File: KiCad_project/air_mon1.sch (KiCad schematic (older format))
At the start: 36 parts, among them J1 USB_OTG, J2 Conn_01x06_Female, M1 Fan, Q1 2N7000, Q2 2N7000, SW1 SW_SPST, U1 LF33_TO220, U2 MH-Z19, U3 AM2320, U4 MSP430G2553_PW20

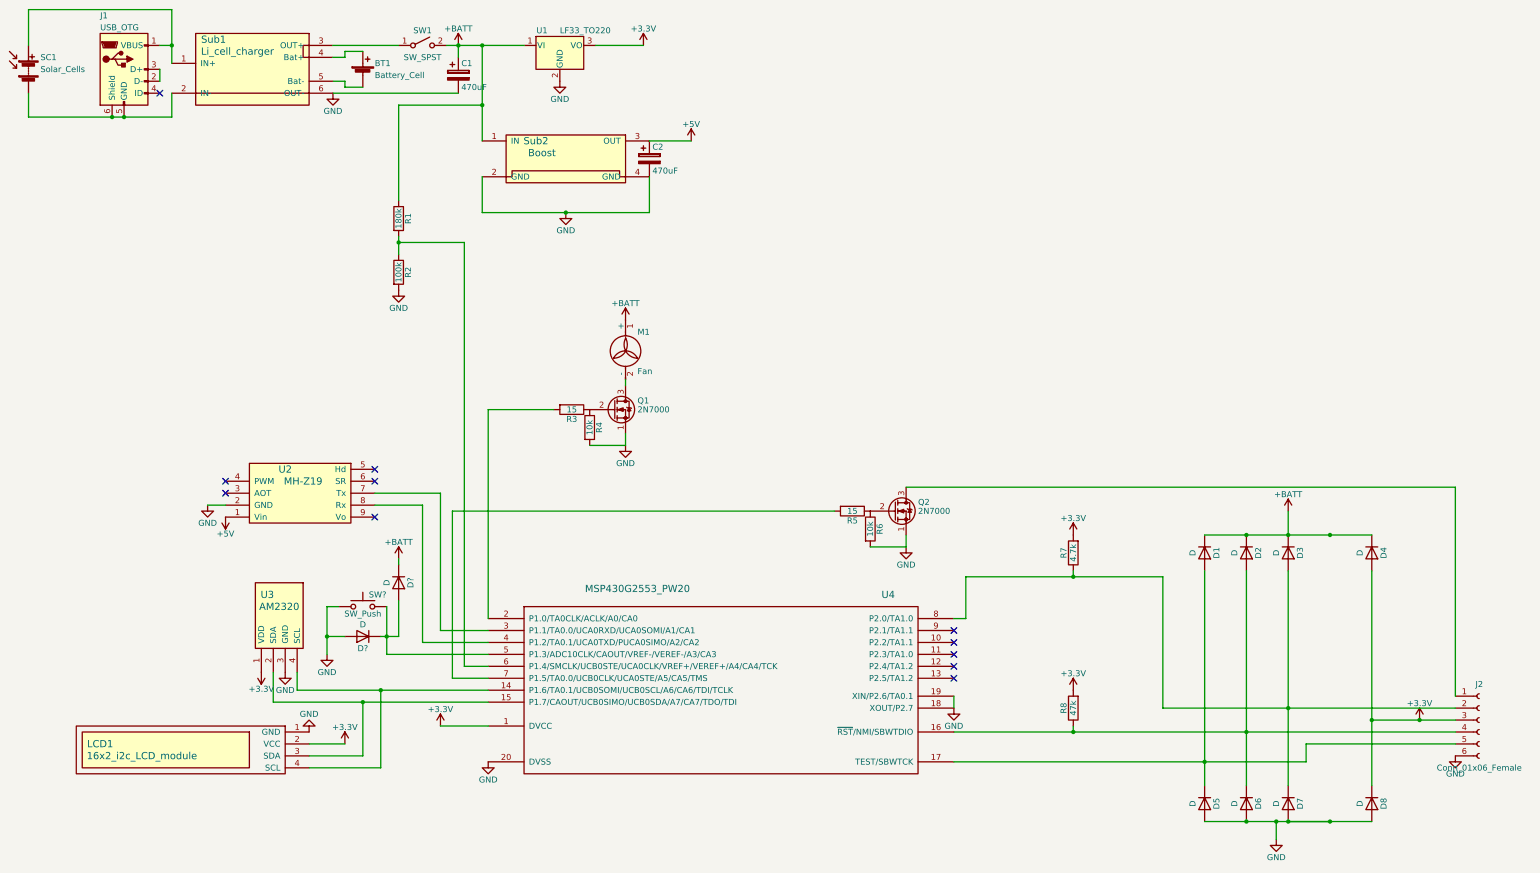
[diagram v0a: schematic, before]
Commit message: Replaced boost module
Use step-up module with Enable pin to control power of CO2 sensor
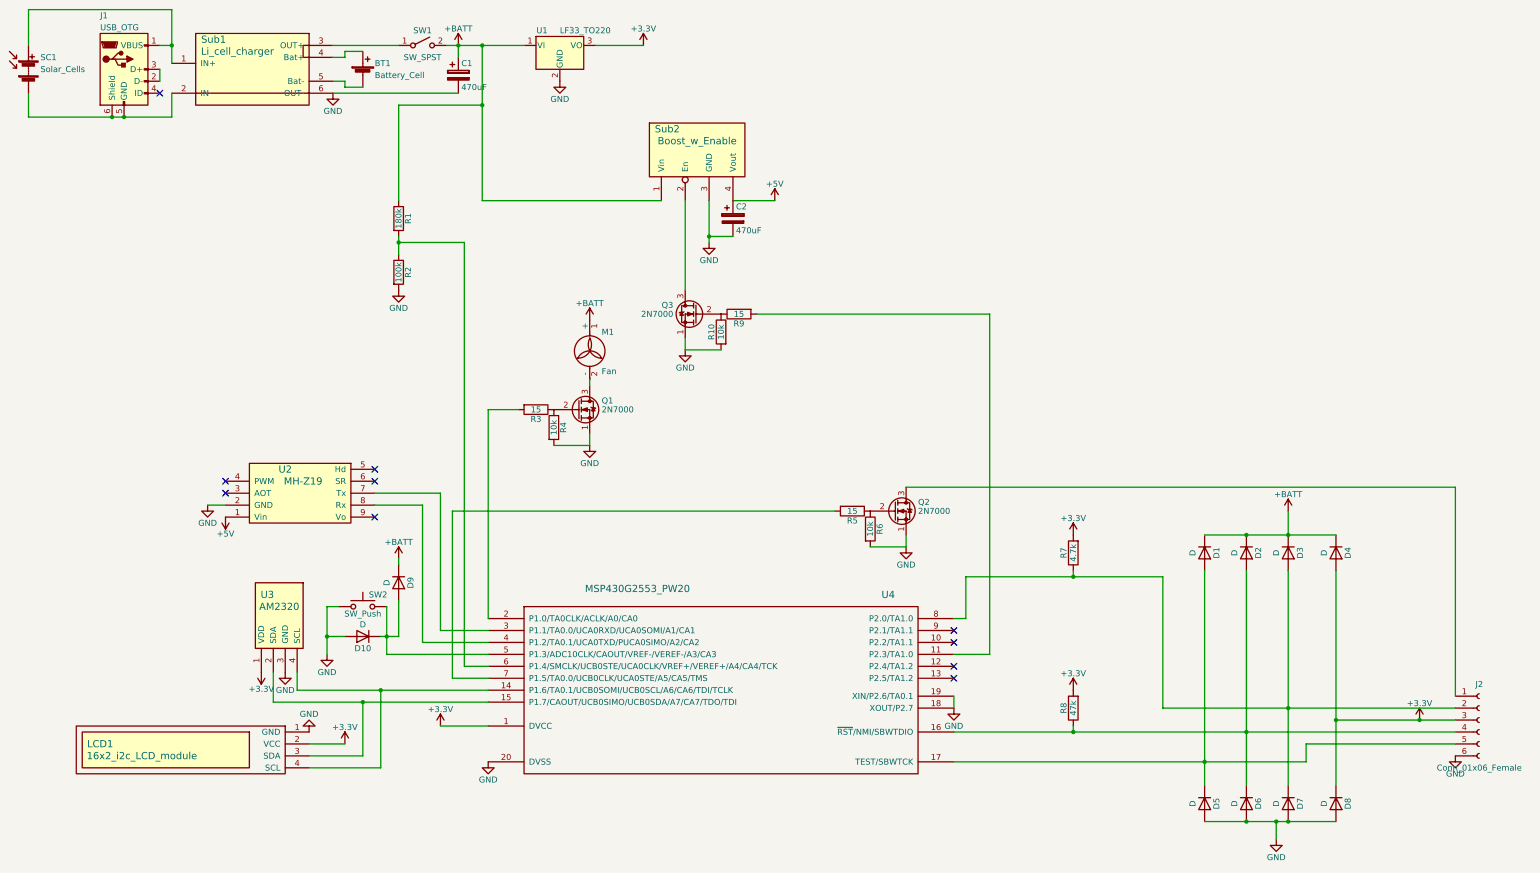
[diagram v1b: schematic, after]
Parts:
- removed Sub2: Boost, symbol Boost
- added Q3: 2N7000, TO_SOT_Packages_THT:TO-92_Molded_Narrow, symbol 2N7000
- added R10: 10k, symbol R
- added R9: 15, symbol R
- added Sub2: Boost_w_Enable, symbol Boost_w_Enable
- gave numbers to parts that had none: 3
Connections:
- net +5V: now also Sub2.4 (Vout)
- net +BATT: now also Sub2.1 (Vin)
- net GND: now also Q3.1 (S), R10.2, Sub2.3 (GND)
- net at U4.11 (P2.3/TA1.0): now also R9.2
- new net: Q3.3 (D), Sub2.2 (En)
- new net: Q3.2 (G), R10.1, R9.1
- no-connect marks 11 -> 10
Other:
- moved on the sheet: C2, D4, D8, M1, Q1, R3, R4
